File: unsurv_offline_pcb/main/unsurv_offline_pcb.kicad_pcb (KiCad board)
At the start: 4 copper layers, 35 x 50 mm, 60 parts, among them J1 10103594-0001LF, J2 S2B-PH-SM4-TB_LF__SN_, J3 1.27mm_female_connector, Q1 Q_PMOS_GSD, Q2 UMH3N, U1 MCP73831-2-OT, U2 APX803L20, U3 NCP59800, U4 MPU-6050_NRND, U5 ESP32-WROOM-32, U6 ublox_SAM-M8Q, U7 CH340G

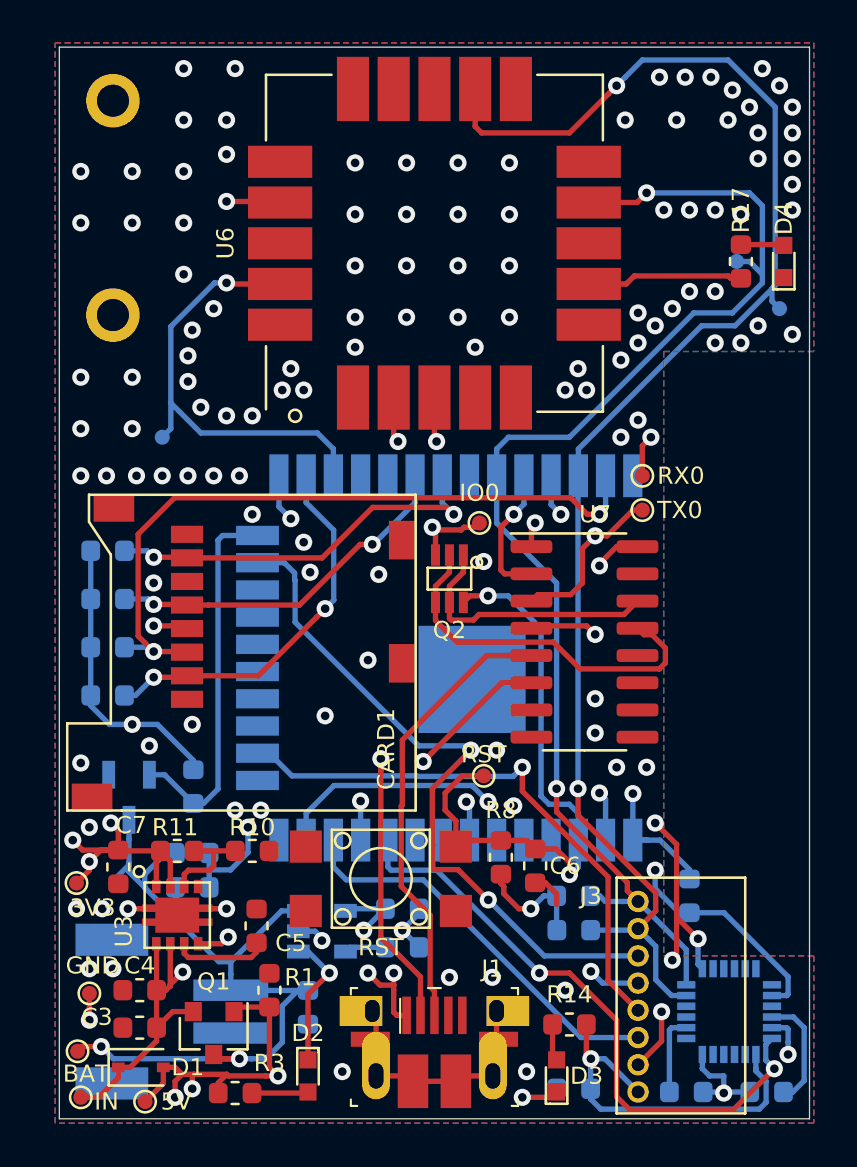
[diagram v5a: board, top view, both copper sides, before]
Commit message: fixed NCP59800 footprint
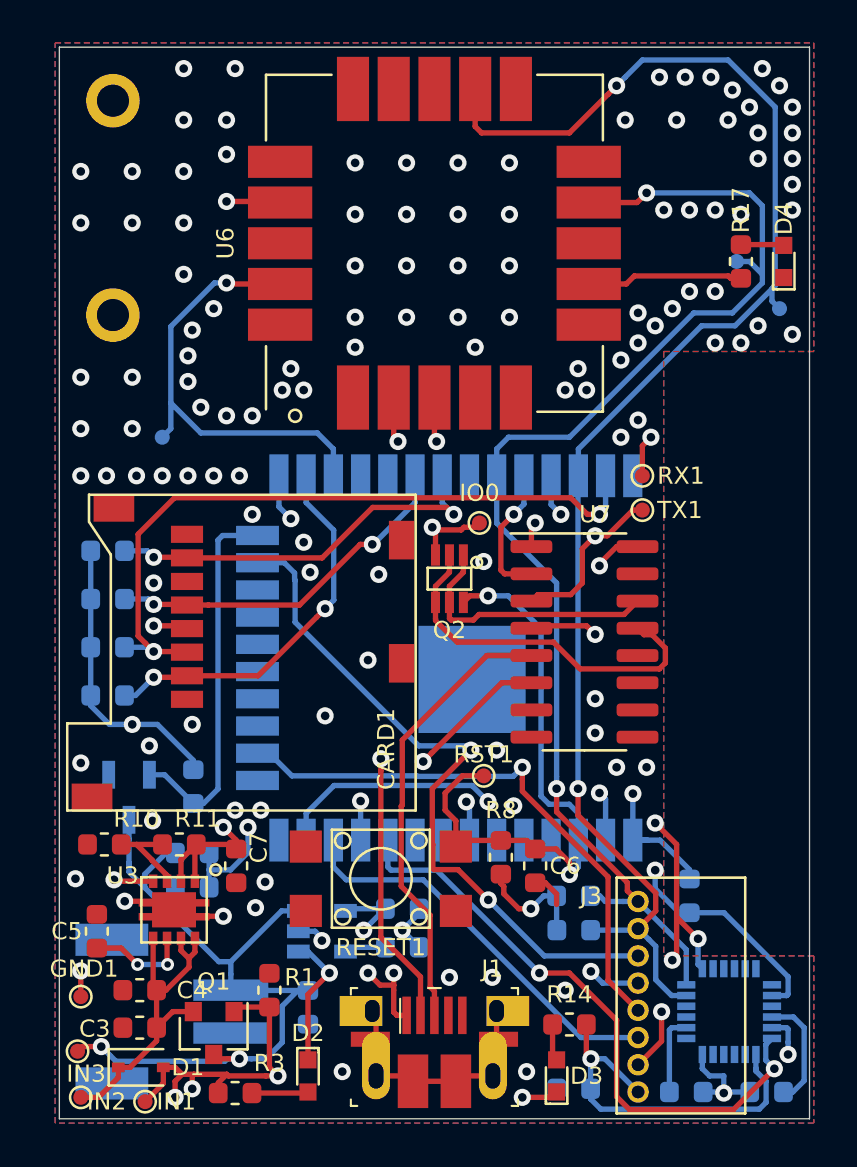
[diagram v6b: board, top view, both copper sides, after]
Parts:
- removed 3V3: TestPoint, unsurv_offline_pcb_footprints:TestPoint_Pad_D0.7mm
- moved C5 7.45 mm to (76.8, 116.2)
- moved R10 6.91 mm to (77.1, 112.2), turned to 0 degrees
- moved C7 5.50 mm to (83.2, 113.2)
- moved GND1 0.43 mm to (76.0, 119.3)
- moved R11 0.32 mm to (80.6, 112.2), turned to 0 degrees
- moved U3 0.29 mm to (80.3, 115.2)
- renumbered GINT to GINT1, GND to GND1, 5V to IN1, IN to IN2, BAT to IN3, RST to RESET1, RST to RST1, RX0 to RX1, SCL to SCL1, SDA to SDA1, TX0 to TX1
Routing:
- net +3V3: track 75.2 -> 70.0 mm, vias 14 -> 12
- net Net-(C3-Pad1): track 19.4 -> 16.3 mm, vias 2 -> 0
- net GND: track 40.9 -> 43.1 mm
- net +BATT: track 36.7 -> 35.6 mm
- net Net-(C5-Pad1): track 4.44 -> 4.84 mm, vias 0 -> 2

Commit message: charging circuit cleanup + new GPS
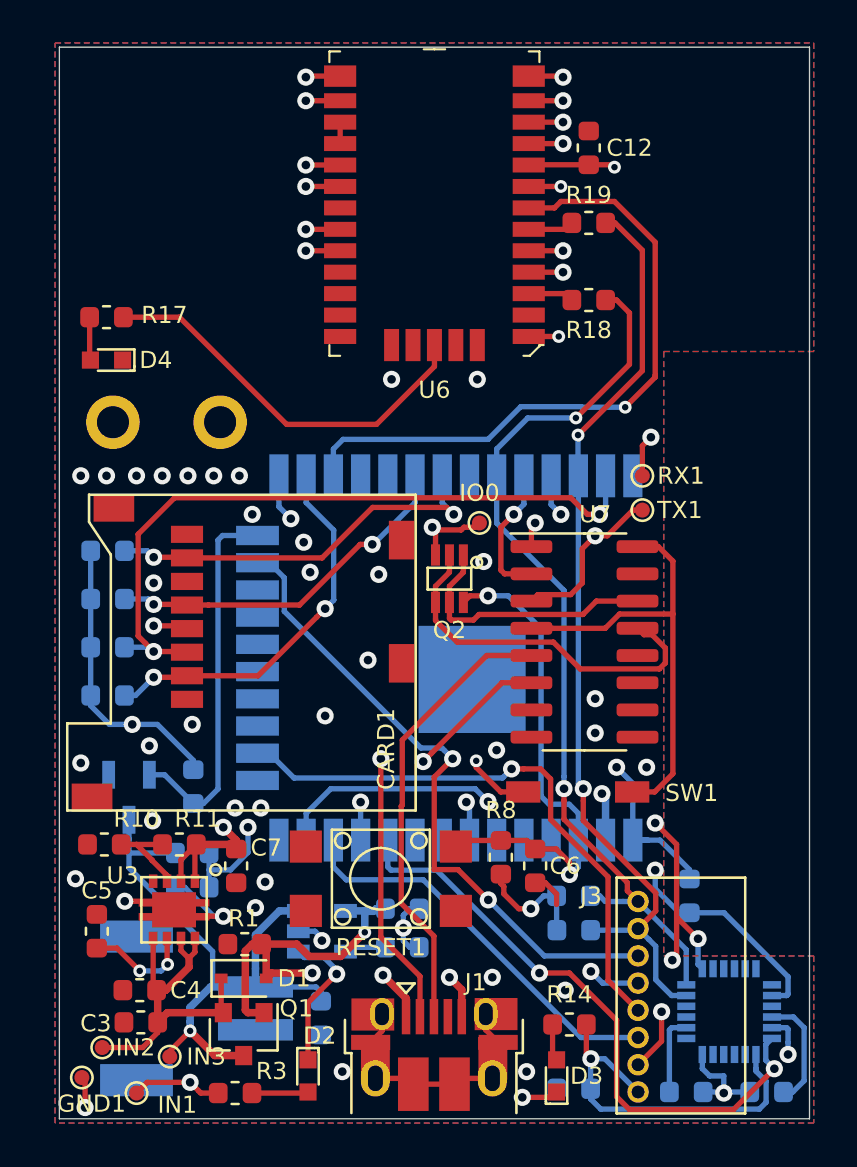
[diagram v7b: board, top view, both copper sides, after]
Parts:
- removed GINT1, RST1, SCL1, SDA1: TestPoint, unsurv_offline_pcb_footprints:TestPoint_Pad_D0.7mm
- added C12: 2.2yF, Capacitor_SMD:C_0603_1608Metric, F.Cu at (99.7, 79.7)
- added R18: 220, Resistor_SMD:R_0603_1608Metric, F.Cu at (99.7, 86.8)
- added R19: 220, Resistor_SMD:R_0603_1608Metric, F.Cu at (99.7, 83.2)
- added SW1: SW_DIP_x01, unsurv_offline_pcb_footprints:CHS-01TA, F.Cu at (101.7, 109.8)
- J1: value 10103594-0001LF -> USB_B_Micro; footprint digikey-footprints:USB_Micro_B_Female_10103594-0001LF -> Connector_USB:USB_Micro-B_Amphenol_10103594-0001LF_Horizontal
- U6: value ublox_SAM-M8Q -> CAM-M8C-0-10; footprint unsurv_offline_pcb_footprints:ublox_SAM-M8Q_HandSolder -> digikey-footprints:GPS_Module_CAM-M8C-0
- moved D4 31.9 mm to (77.2, 89.6), turned to 180 degrees
- moved R17 29.7 mm to (77.2, 87.6), turned to 180 degrees
- moved H1 15.8 mm to (82.5, 92.5)
- moved D1 6.35 mm to (83.6, 118.5)
- moved H2 5.00 mm to (77.5, 92.5)
- moved IN3 4.31 mm to (80.2, 122.1)
- moved GND1 3.78 mm to (76.0, 123.1)
- moved IN2 2.53 mm to (77.0, 121.7)
- moved R1 2.44 mm to (83.7, 116.8), turned to 0 degrees
- moved U6 1.65 mm to (92.5, 82.5), turned to 180 degrees
- moved Q1 1.40 mm to (83.6, 121.0)
- moved J2 1.16 mm to (84.2, 119.8)
- moved J1 1.00 mm to (92.5, 122.0)
- moved C2 0.78 mm to (87.2, 120.3)
- moved IN1 0.57 mm to (78.6, 123.8)
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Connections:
- U6 pad 1: GND -> +3V3
- U6 pad 12: SCL -> GND
- U6 pad 13: Net-(U6-Pad13) -> GND
- U6 pad 14: Net-(U6-Pad14) -> GND
- U6 pad 16: GND -> Net-(U6-Pad16)
- U6 pad 17: +3V3 -> Net-(U6-Pad16)
- U6 pad 18: Net-(U6-Pad18) -> GND
- U6 pad 19: 16 -> GND
- U6 pad 2: +3V3 -> Net-(U6-Pad2)
- U6 pad 20: GND -> Net-(U6-Pad20)
- U6 pad 3: +3V3 -> Net-(R18-Pad1)
- U6 pad 6: GND -> Net-(R19-Pad1)
- U6 pad 7: Net-(R17-Pad1) -> 16
- U6 pad 8: Net-(U6-Pad8) -> +3V3
- U6 pad 9: SDA -> +3V3
- U7 pad 16: +3V3 -> Net-(SW1-Pad1)
- U7 pad 4: +3V3 -> Net-(SW1-Pad1)
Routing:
- net SCL: track 71.2 -> 43.8 mm
- net GND: track 43.1 -> 66.4 mm, vias 130 -> 60
- net Net-(SW1-Pad1): track 0.00 -> 21.1 mm
- net SDA: track 60.2 -> 42.6 mm
- net Net-(J1-PadSH): track 11.9 -> 0.00 mm
- net Net-(R17-Pad1): track 7.30 -> 18.7 mm
- net 16: track 21.0 -> 30.8 mm
- net Net-(J1-Pad6): track 0.00 -> 8.78 mm
- net +BATT: track 35.6 -> 29.2 mm, vias 2 -> 1
- net RESET: track 28.6 -> 23.7 mm
- net +3V3: track 70.0 -> 67.7 mm, vias 12 -> 11
- net Net-(R19-Pad1): track 0.00 -> 2.14 mm
- net Net-(R18-Pad1): track 0.00 -> 2.14 mm
- net 15: track 32.4 -> 30.5 mm
- net 35: track 19.8 -> 18.3 mm
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
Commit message: improved routing + less vias
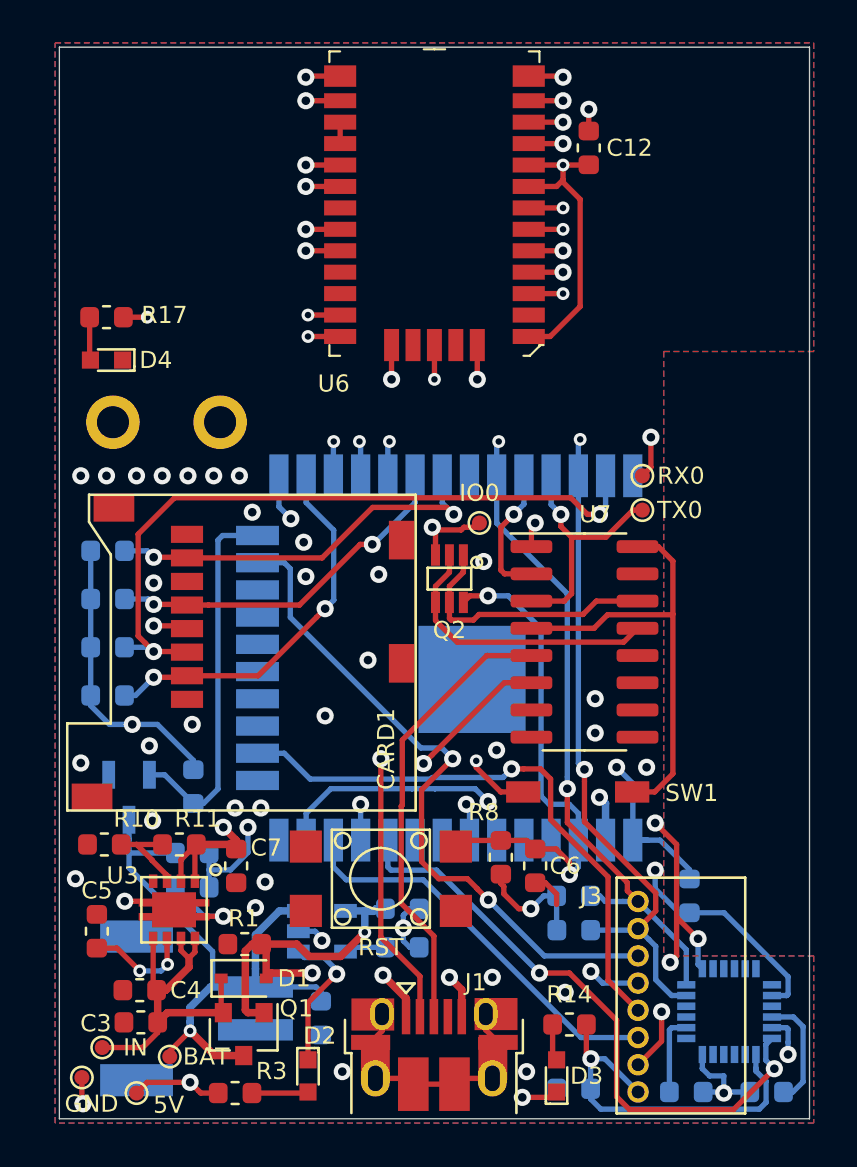
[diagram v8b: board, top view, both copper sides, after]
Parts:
- removed R18, R19: 220, Resistor_SMD:R_0603_1608Metric
- renumbered IN1 to 5V, IN3 to BAT, GND1 to GND, IN2 to IN, RESET1 to RST, RX1 to RX0, TX1 to TX0
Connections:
- U5 pad 27: 16 -> RX2
- U5 pad 28: Net-(U5-Pad28) -> TX2
- U6 pad 25: Net-(U6-Pad25) -> TX2
- U6 pad 26: Net-(U6-Pad26) -> RX2
- U6 pad 3: Net-(R18-Pad1) -> SDA
- U6 pad 6: Net-(R19-Pad1) -> SCL
- U6 pad 7: 16 -> 5
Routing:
- net 16: track 30.8 -> 0.00 mm, vias 1 -> 0
- net 5: track 0.00 -> 30.0 mm, vias 0 -> 2
- net TX2: track 0.00 -> 13.1 mm, vias 0 -> 2
- net RX2: track 0.00 -> 8.50 mm, vias 0 -> 2
- net +3V3: track 67.7 -> 75.1 mm, vias 11 -> 9
- net SDA: track 42.6 -> 46.7 mm, vias 2 -> 3
- net GND: track 66.4 -> 70.6 mm, vias 60 -> 61
- net DTR: track 17.5 -> 13.4 mm
- net SCL: track 43.8 -> 47.4 mm, vias 2 -> 3
- net Net-(R19-Pad1): track 2.14 -> 0.00 mm
- net Net-(R18-Pad1): track 2.14 -> 0.00 mm
- net 15: track 30.5 -> 31.6 mm
- net Net-(R17-Pad1): track 18.7 -> 19.4 mm, vias 0 -> 2
- net TX0: track 12.1 -> 11.9 mm, vias 2 -> 1
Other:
- net class Default: clearance 0.1 -> 0.15
- rule trace_clearance: 0.1 -> 0.15
